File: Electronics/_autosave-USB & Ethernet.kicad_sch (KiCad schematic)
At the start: 12 parts, among them IC4 USB2512B-AEZG, J22 USB_A, J23 USB_A, Y3 30MHz

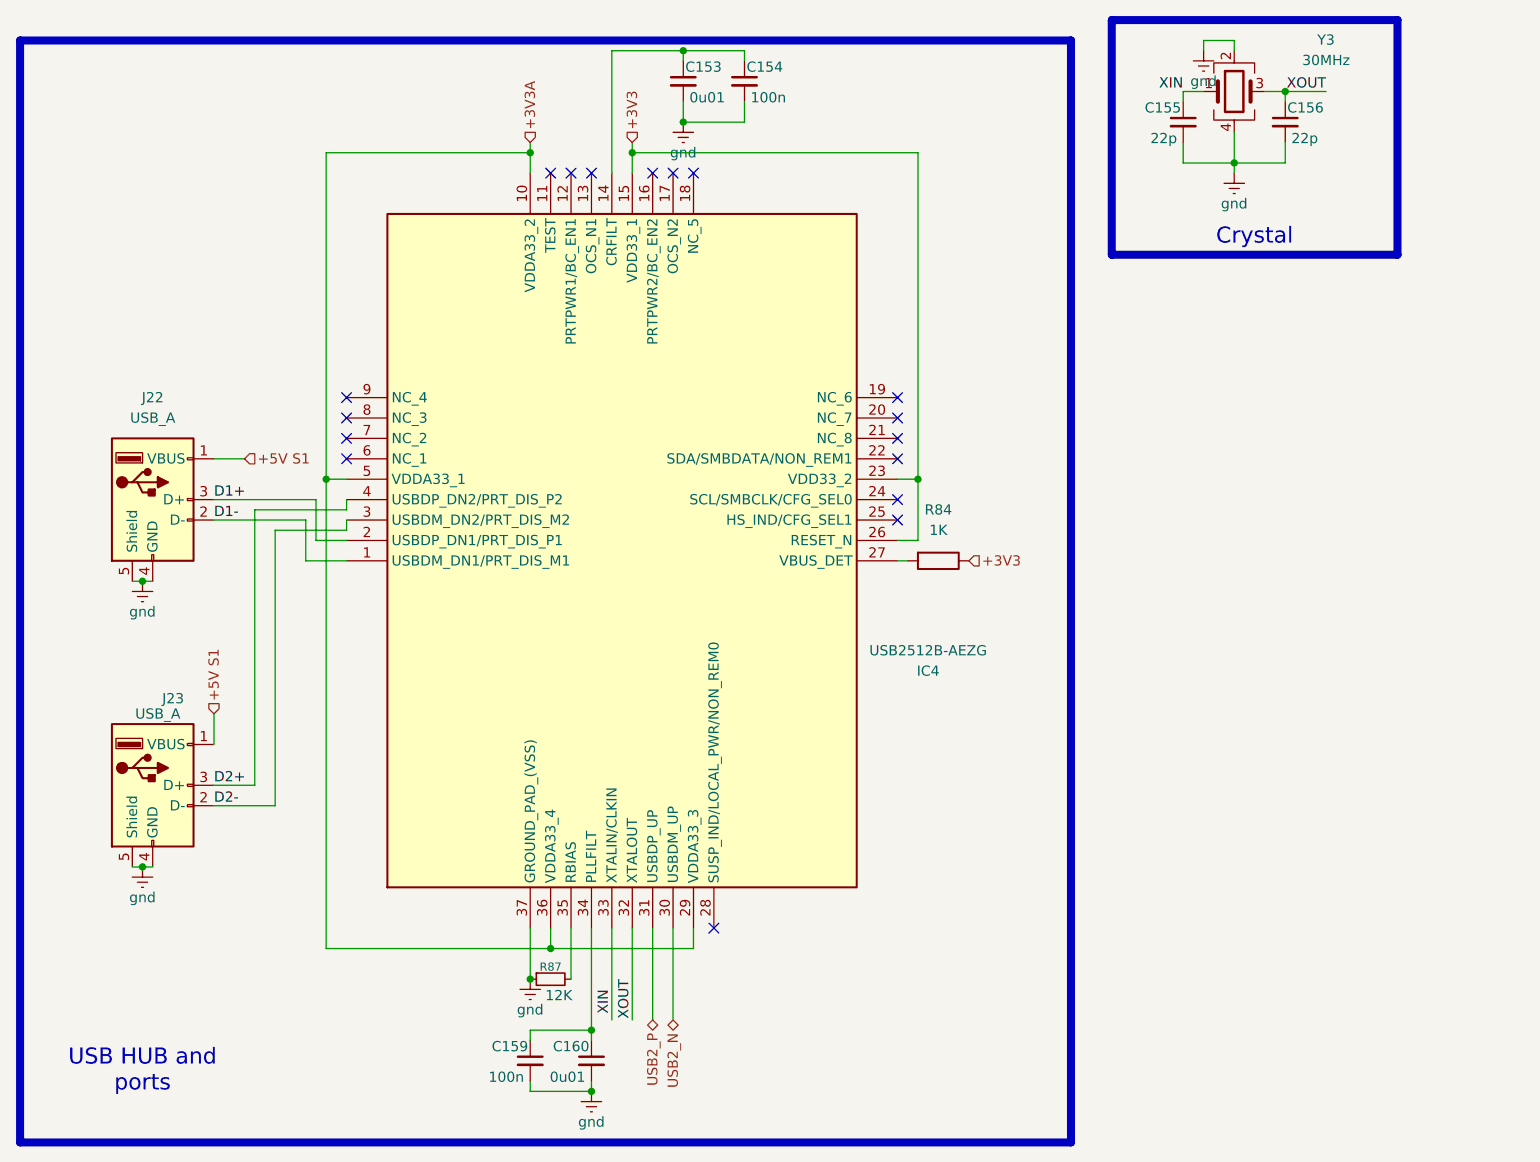
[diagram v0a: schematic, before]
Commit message: Power symbols changed and sata hub fixed schem
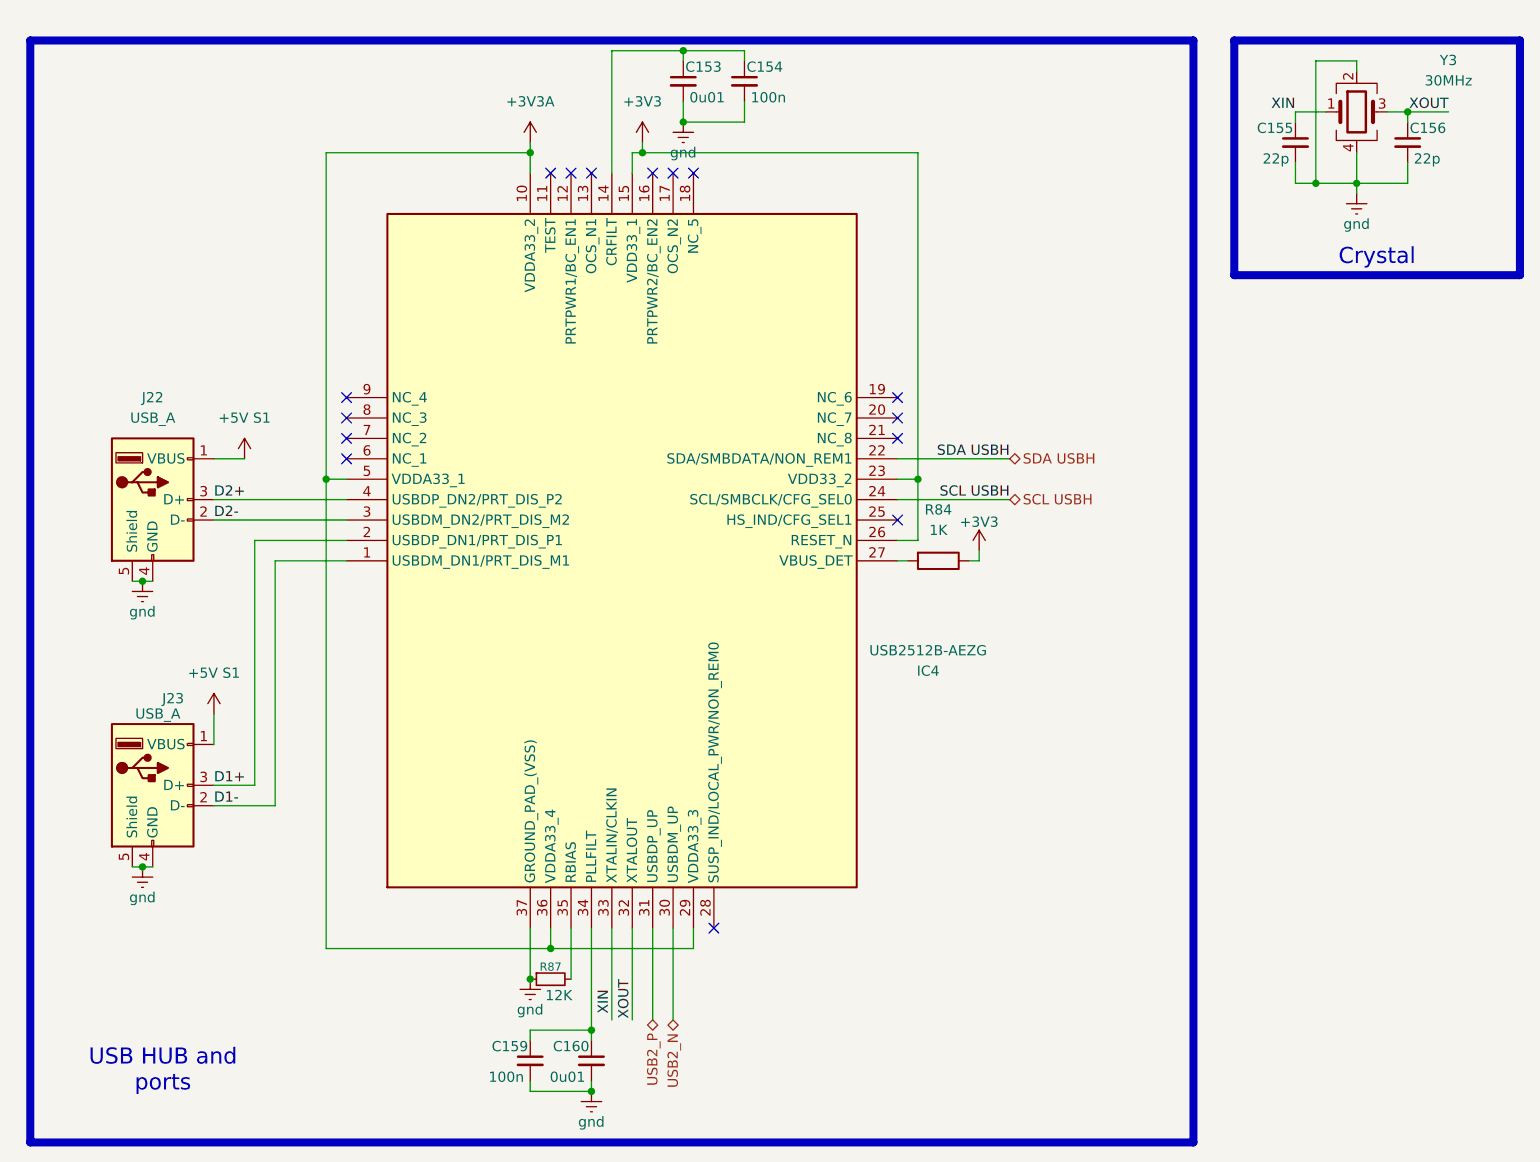
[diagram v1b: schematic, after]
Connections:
- net D1+: now also J23.3 (D+); no longer J22.3 (D+)
- net D1-: now also J23.2 (D-); no longer J22.2 (D-)
- net D2+: now also J22.3 (D+); no longer J23.3 (D+)
- net D2-: now also J22.2 (D-); no longer J23.2 (D-)
- net SDA USBH: now reaches IC4.22 (SDA/SMBDATA/NON_REM1)
- net SCL USBH: now reaches IC4.24 (SCL/SMBCLK/CFG_SEL0)
- no-connect marks 17 -> 15
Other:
- moved on the sheet: C155, C156, Y3
